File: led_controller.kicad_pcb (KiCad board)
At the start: 2 copper layers, 88.9 x 46.2 mm, 83 parts, among them J1 Screw_Terminal_01x02, J10 Conn_01x03, J2 SJ-3524-SMT, J3 Conn_01x03, J4 Conn_01x03, J5 Conn_01x03, J6 Conn_01x03, J7 Conn_01x03, J8 Conn_01x03, J9 Conn_01x03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

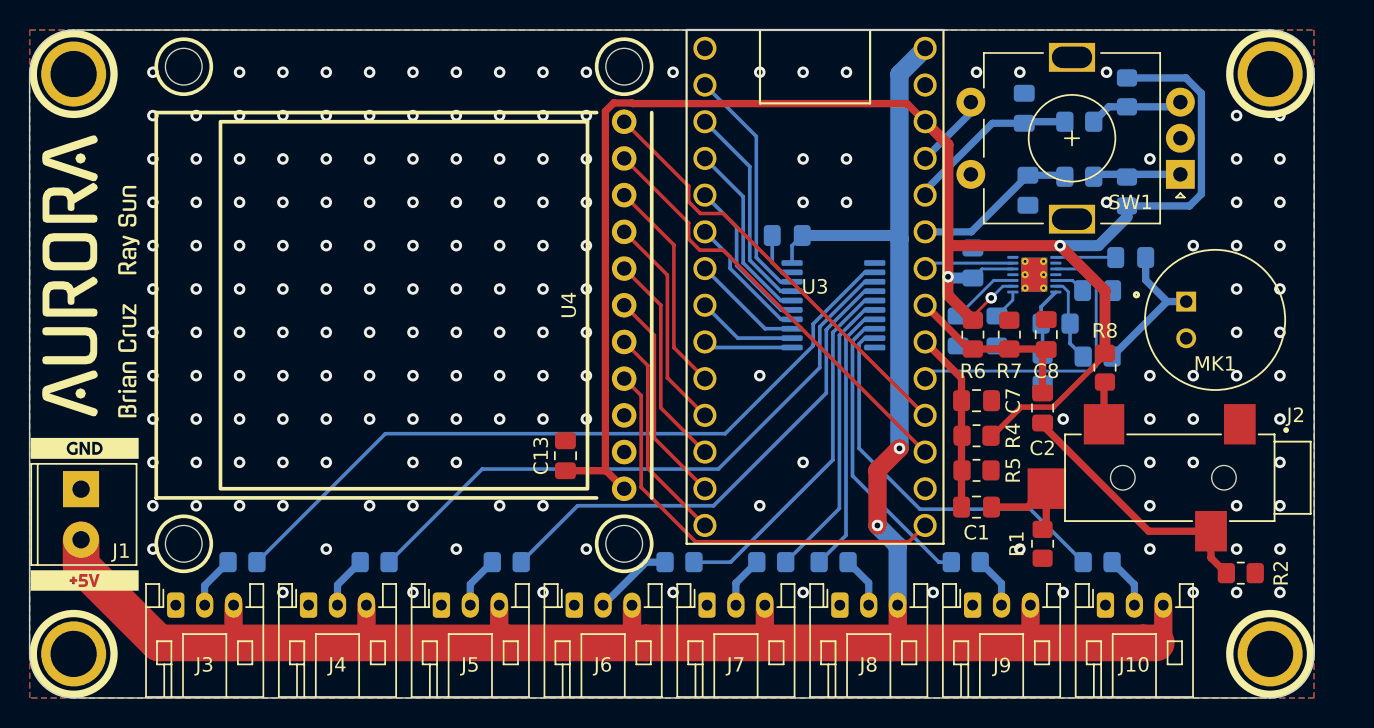
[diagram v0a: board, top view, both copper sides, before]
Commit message: Fix audio jack pinout and route jack insertion pin
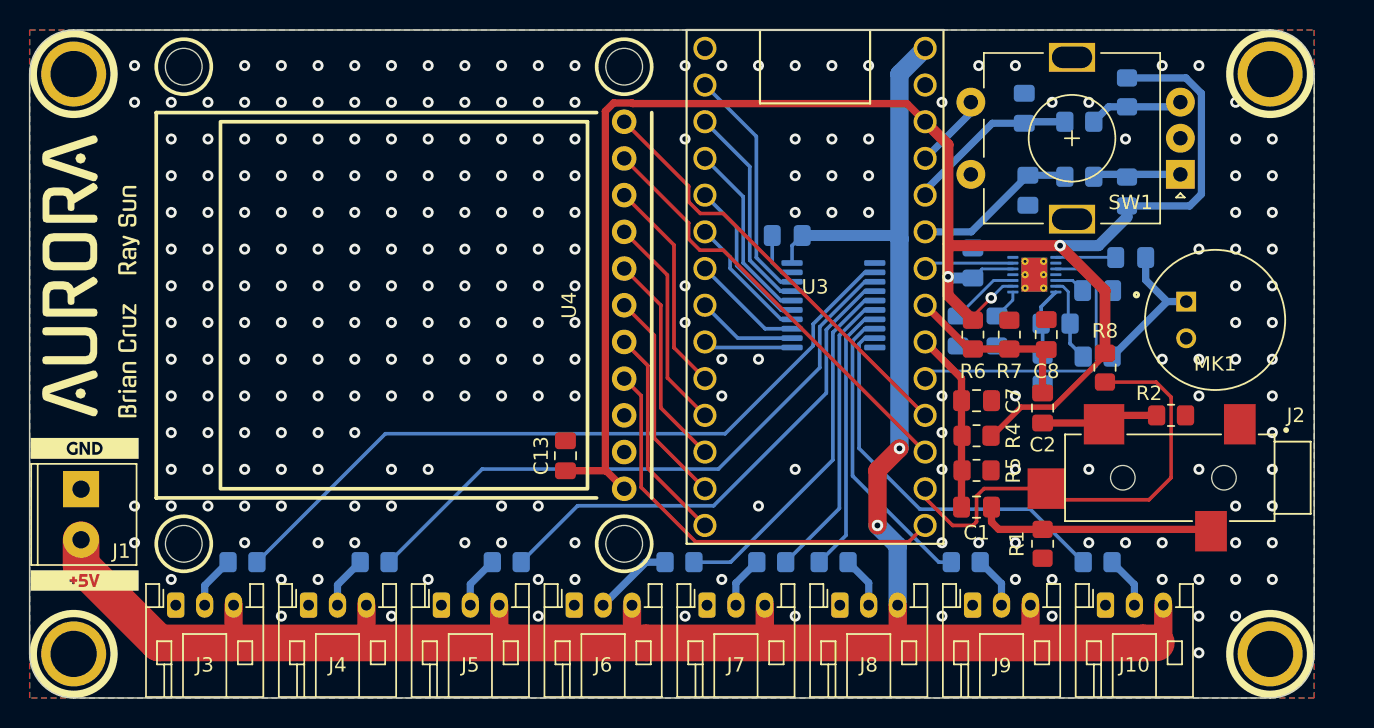
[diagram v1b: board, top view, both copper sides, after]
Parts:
- C4: value 470n -> 0.47u
- moved R2 11.9 mm to (169.2, 113.8)
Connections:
- C1 pad 1: /AUD_L_ADC -> /AUD_R_ADC
- C1 pad 2: /AUD_L -> /AUD_R
- C2 pad 1: /AUD_R_ADC -> /AUD_L_ADC
- C2 pad 2: /AUD_R -> /AUD_L
- C7 pad 1: /AUD_L_ADC -> /AUD_R_ADC
- C8 pad 1: /AUD_R_ADC -> /AUD_L_ADC
- J2 pad 2: Net-(J2-Pad2) -> /AUD_L
- J2 pad 4: /AUD_L -> /AUD_DET
- R1 pad 1: /AUD_L -> /AUD_R
- R2 pad 1: /AUD_R -> /AUD_L
- R4 pad 2: /AUD_L_ADC -> /AUD_R_ADC
- R5 pad 1: /AUD_L_ADC -> /AUD_R_ADC
- R6 pad 2: /AUD_R_ADC -> /AUD_L_ADC
- R7 pad 1: /AUD_R_ADC -> /AUD_L_ADC
- R8 pad 2: Net-(J2-Pad2) -> /AUD_DET
- U3 pad 21: unconnected-(U3-Pad21) -> /AUD_DET
- U3 pad 25: /AUD_L_ADC -> /AUD_R_ADC
- U3 pad 26: /AUD_R_ADC -> /AUD_L_ADC
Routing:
- net /AUD_DET: track 0.00 -> 32.2 mm
- net Net-(J2-Pad2): track 2.95 -> 0.00 mm
- net /AUD_R: track 18.2 -> 16.8 mm
- net /AUD_L: track 7.24 -> 8.54 mm
- net GND: vias 174 -> 242

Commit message: Enter pads at right angles for aesthetics
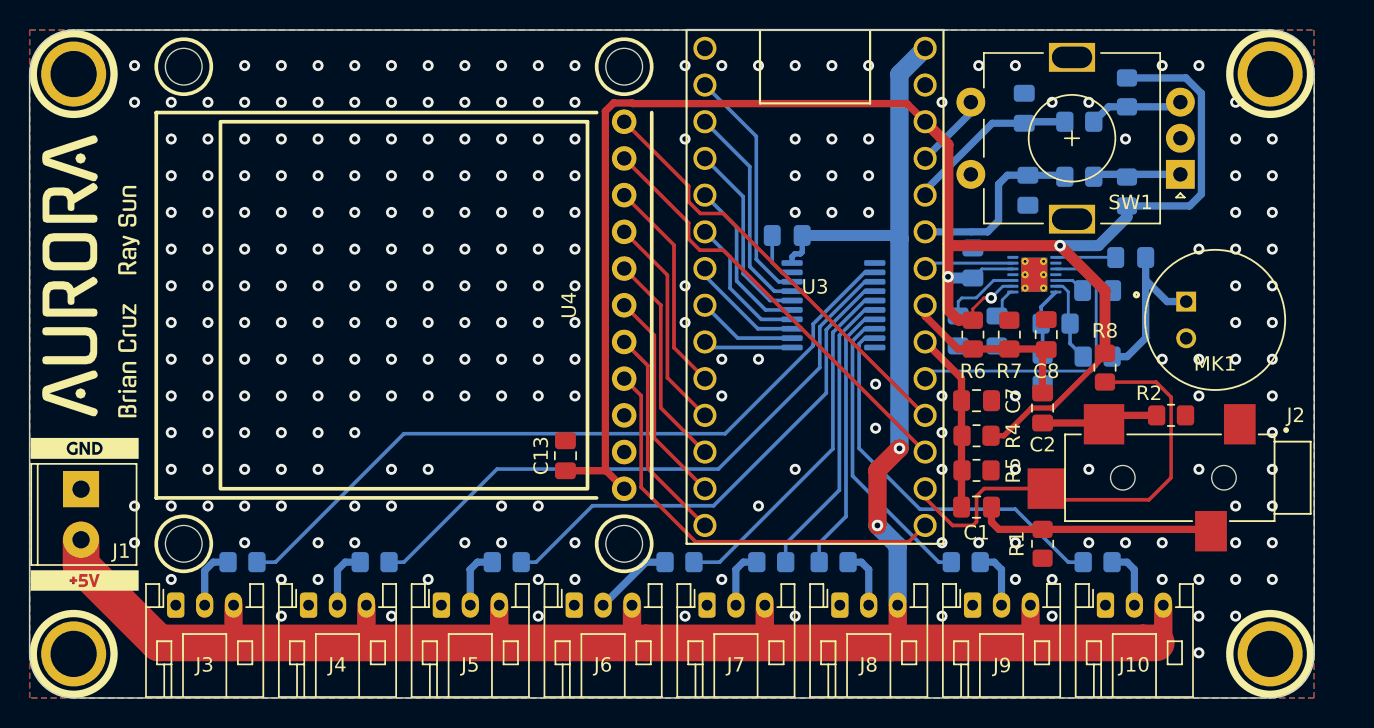
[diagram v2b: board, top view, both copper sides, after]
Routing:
- net /ENCODER_A: track 11.3 -> 12.8 mm
- net Net-(C3-Pad2): track 10.4 -> 11.8 mm
- net +3V3: track 127.3 -> 128.2 mm
- net Net-(U2-Pad14): track 9.00 -> 9.80 mm
- net Net-(U2-Pad15): track 10.9 -> 11.5 mm
- net /LED_OUT_2: track 3.60 -> 4.22 mm
- net /LED_OUT_7: track 3.61 -> 4.22 mm
- net /LED_OUT_1: track 3.62 -> 4.23 mm
- net /LED_OUT_0: track 3.64 -> 4.25 mm
- net Net-(C6-Pad2): track 4.80 -> 5.38 mm
- net /LED_OUT_6: track 3.59 -> 4.15 mm
- net /LED_OUT_4: track 3.57 -> 4.12 mm
- net /LED_OUT_5: track 3.57 -> 4.11 mm
- net GND: vias 242 -> 244

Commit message: Rearrange some analog pins, tweak routing
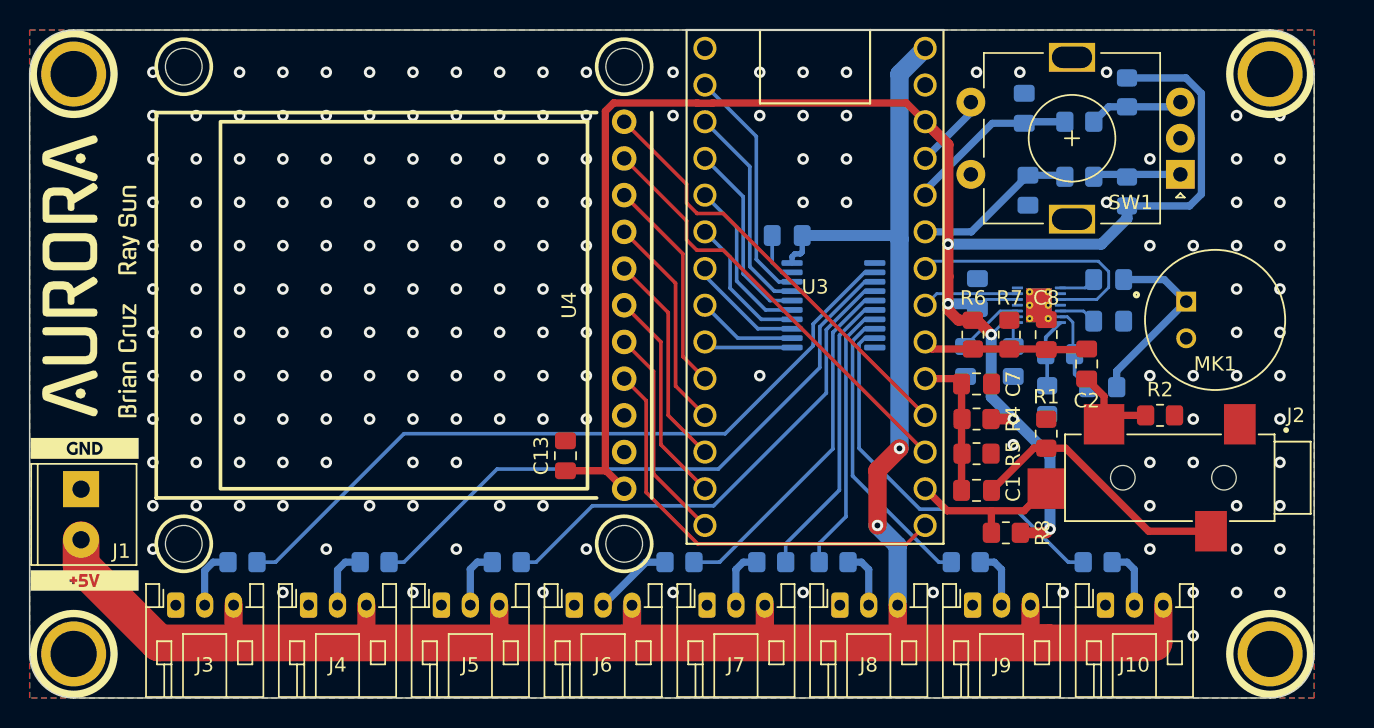
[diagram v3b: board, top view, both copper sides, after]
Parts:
- moved R8 13.3 mm to (157.7, 121.9), turned to 180 degrees
- moved R1 7.62 mm to (160.5, 115.1), turned to 90 degrees
- moved C2 4.31 mm to (163.3, 110.2)
- moved C4 2.40 mm to (158.2, 110.1)
- moved C5 2.25 mm to (164.8, 107.3)
- moved C6 2.17 mm to (154.9, 110.1)
- moved C3 2.16 mm to (164.8, 104.4)
- moved R21 2.14 mm to (161.5, 109.6)
- moved R22 2.14 mm to (160.6, 112.7)
- moved R3 2.14 mm to (164.4, 111.8)
- moved U1 2.14 mm to (160.0, 106.2)
- moved C12 2.14 mm to (155.8, 105.4)
- moved C1 1.16 mm to (155.7, 119.0)
- moved C7 1.16 mm to (155.7, 111.6)
- moved R5 1.16 mm to (155.7, 116.4)
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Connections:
- U3 pad 24: /MIC_GAIN -> /AUD_R_ADC
- U3 pad 25: /AUD_R_ADC -> /AUD_L_ADC
- U3 pad 26: /AUD_L_ADC -> /MIC_ADC
- U3 pad 27: /MIC_ADC -> /MIC_GAIN
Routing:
- net /AUD_DET: track 32.2 -> 11.2 mm
- net /MIC_GAIN: track 21.2 -> 18.0 mm
- net /AUD_R_ADC: track 12.5 -> 10.0 mm
- net +5V: track 149.0 -> 151.4 mm
- net /AUD_R: track 16.8 -> 19.0 mm
- net /AUD_L_ADC: track 13.2 -> 11.4 mm
- net Net-(C3-Pad1): track 4.15 -> 2.54 mm
- net /AUD_L: track 8.54 -> 6.98 mm
- net /ENCODER_A: track 12.8 -> 11.3 mm
- net Net-(C3-Pad2): track 11.8 -> 12.9 mm
- net Net-(C6-Pad2): track 5.38 -> 4.64 mm
- net +3V3: track 128.2 -> 128.4 mm, vias 3 -> 5
- net GND: vias 244 -> 176

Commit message: some more tweaks
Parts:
- moved J2 2.29 mm to (175.1, 118.1)
- moved R2 2.29 mm to (170.7, 113.8)
- moved C1 0.87 mm to (156.6, 119.0)
- moved C7 0.87 mm to (156.6, 111.6)
- moved R1 0.87 mm to (161.4, 115.1)
- moved R4 0.87 mm to (156.6, 114.0)
- moved R5 0.87 mm to (156.6, 116.4)
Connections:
- U3 pad 22: /CS_SD -> /AUD_R_ADC
- U3 pad 23: /BACKLIGHT -> /AUD_L_ADC
- U3 pad 24: /AUD_R_ADC -> /CS_SD
- U3 pad 25: /AUD_L_ADC -> /BACKLIGHT
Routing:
- net GND: track 3.52 -> 0.00 mm, vias 176 -> 175
- net /AUD_L_ADC: track 11.4 -> 14.6 mm
- net /CS_SD: track 30.0 -> 27.1 mm
- net /BACKLIGHT: track 30.0 -> 27.1 mm
- net /AUD_DET: track 11.2 -> 13.5 mm
- net /AUD_R: track 19.0 -> 20.2 mm
- net /AUD_L: track 6.98 -> 7.92 mm
- net +3V3: track 128.4 -> 127.5 mm
- net /AUD_R_ADC: track 10.0 -> 10.8 mm
- net Net-(R15-Pad2): track 34.8 -> 35.6 mm
- net +5V: track 151.4 -> 150.9 mm
